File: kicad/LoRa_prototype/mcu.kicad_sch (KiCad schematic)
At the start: 38 parts, among them SW1 SW_Push, U1 STM32WL55JCIx, X1 32768Hz, X2 TCXO

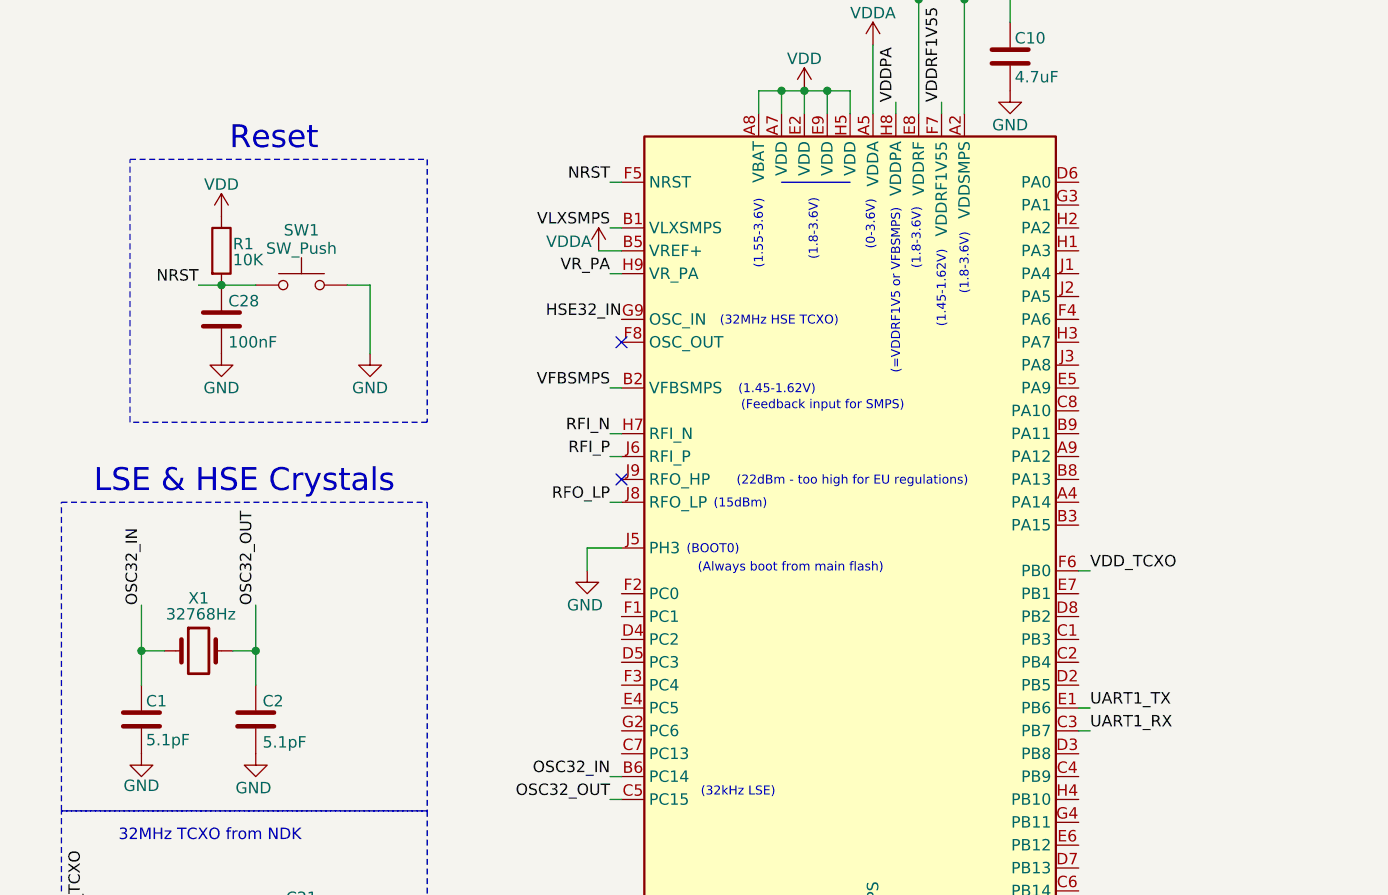
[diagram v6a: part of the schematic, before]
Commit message: Schematic for programming interface done
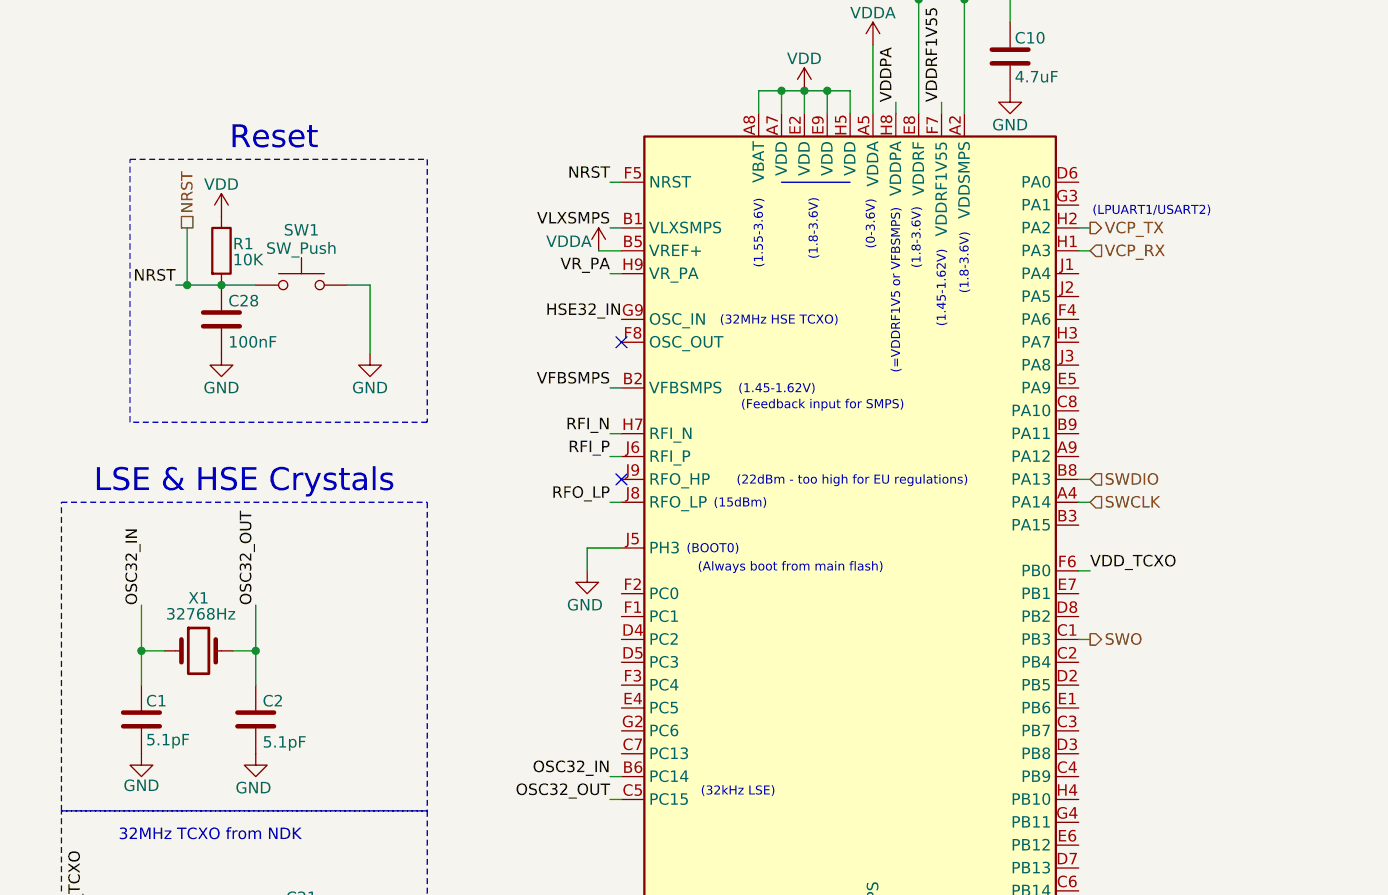
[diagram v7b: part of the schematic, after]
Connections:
- net SWCLK: now reaches U1.A4 (PA14)
- net SWDIO: now reaches U1.B8 (PA13)
- net SWO: now reaches U1.C1 (PB3)
- net VCP_RX: now reaches U1.H1 (PA3)
- net VCP_TX: now reaches U1.H2 (PA2)
- net UART1_RX: no longer names the net of U1.C3 (PB7)
- net UART1_TX: no longer names the net of U1.E1 (PB6)
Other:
- note added: "(LPUART1/USART2)"
